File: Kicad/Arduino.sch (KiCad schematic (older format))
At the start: 5 parts

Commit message: Ready for Rev3 First layout review
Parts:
- removed D4: RGB_LED, ~, symbol RGB_LED
- added D4: LB_RGBLED, ~, symbol LB_RGBLED
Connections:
- wire segments 21 -> 26
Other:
- note added: "Changed model (3 units, pins = datasheet)"
- note added: "Connected 2nd Ard GND."
- moved on the sheet: R13, R14
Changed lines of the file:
@@
 Sheet 3 7
 Title ""
-Date "11 oct 2014"
+Date "18 oct 2014"
 Rev ""
 Comp ""
@@
 Text HLabel 2500 3550 0    60   Output ~ 0
 PumpDown
-Text HLabel 6400 3800 2    60   Output ~ 0
+Text HLabel 6400 2800 2    60   Output ~ 0
 ~RESET
-Text HLabel 6450 4200 2    60   Input ~ 0
+Text HLabel 6450 3000 2    60   Input ~ 0
 ~DR
 Wire Wire Line
-	5750 4200 6450 4200
+	5750 3000 6450 3000
 Text HLabel 2500 2450 0    60   Output ~ 0
 V+_ARD
@@
 	2500 3750 3550 3750
 Wire Wire Line
-	5750 3800 6400 3800
-$Comp
-L RGB_LED D4
-U 1 1 540F4D9B
-P 1750 4250
-F 0 "D4" H 1850 4600 50  0000 L CNN
-F 1 "RGB_LED" H 1750 3650 50  0000 C CNN
-F 2 "~" H 1750 4250 60  0000 C CNN
-F 3 "~" H 1750 4250 60  0000 C CNN
-	1    1750 4250
-	1    0    0    1
-$EndComp
+	5750 2800 6400 2800
 $Comp
 L R R14
 U 1 1 540F4E5D
-P 2850 4150
-F 0 "R14" V 2930 4150 40  0000 C CNN
-F 1 "499" V 2857 4151 40  0000 C CNN
-F 2 "~" V 2780 4150 30  0000 C CNN
-F 3 "~" H 2850 4150 30  0000 C CNN
-	1    2850 4150
+P 2850 4350
+F 0 "R14" V 2930 4350 40  0000 C CNN
+F 1 "499" V 2857 4351 40  0000 C CNN
+F 2 "~" V 2780 4350 30  0000 C CNN
+F 3 "~" H 2850 4350 30  0000 C CNN
+	1    2850 4350
 	0    -1   -1   0
 $EndComp
@@
 L R R13
 U 1 1 540F4E9E
-P 2850 4350
-F 0 "R13" V 2930 4350 40  0000 C CNN
-F 1 "499" V 2857 4351 40  0000 C CNN
-F 2 "~" V 2780 4350 30  0000 C CNN
-F 3 "~" H 2850 4350 30  0000 C CNN
-	1    2850 4350
+P 2850 4750
+F 0 "R13" V 2930 4750 40  0000 C CNN
+F 1 "499" V 2857 4751 40  0000 C CNN
+F 2 "~" V 2780 4750 30  0000 C CNN
+F 3 "~" H 2850 4750 30  0000 C CNN
+	1    2850 4750
 	0    -1   -1   0
 $EndComp
@@
 	3550 3950 3100 3950
 Wire Wire Line
-	2600 3950 2100 3950
+	1900 3950 2600 3950
 Wire Wire Line
-	2600 4150 2100 4150
+	1900 4350 2600 4350
 Wire Wire Line
-	2600 4350 2100 4350
+	1900 4750 2600 4750
+Text HLabel 950  4350 0    60   Output ~ 0
+V+_ARD
+$Comp
+L LB_RGBLED D4
+U 1 1 544128B0
+P 1700 3950
+F 0 "D4" H 1700 4050 50  0000 C CNN
+F 1 "LB_RGBLED" H 1700 3850 50  0000 C CNN
+F 2 "~" H 1700 3950 60  0000 C CNN
+F 3 "~" H 1700 3950 60  0000 C CNN
+	1    1700 3950
+	1    0    0    -1
+$EndComp
+$Comp
+L LB_RGBLED D4
+U 2 1 544128BD
+P 1700 4350
+F 0 "D4" H 1700 4450 50  0000 C CNN
+F 1 "LB_RGBLED" H 1700 4250 50  0000 C CNN
+F 2 "~" H 1700 4350 60  0000 C CNN
+F 3 "~" H 1700 4350 60  0000 C CNN
+	2    1700 4350
+	1    0    0    -1
+$EndComp
+$Comp
+L LB_RGBLED D4
+U 3 1 544128C3
+P 1700 4750
+F 0 "D4" H 1700 4850 50  0000 C CNN
+F 1 "LB_RGBLED" H 1700 4650 50  0000 C CNN
+F 2 "~" H 1700 4750 60  0000 C CNN
+F 3 "~" H 1700 4750 60  0000 C CNN
+	3    1700 4750
+	1    0    0    -1
+$EndComp
 Wire Wire Line
-	1350 4150 1200 4150
-Text HLabel 1200 4150 0    60   Output ~ 0
-V+_ARD
+	950  4350 1500 4350
 Wire Wire Line
-	3100 4150 3200 4150
+	1050 3950 1050 4750
 Wire Wire Line
-	3200 4150 3200 4350
+	1050 3950 1500 3950
+Connection ~ 1050 4350
 Wire Wire Line
-	3200 4350 3550 4350
+	1050 4750 1500 4750
+Text Notes 2700 5050 2    60   ~ 0
+Changed model (3 units, pins = datasheet)
 Wire Wire Line
-	3100 4350 3100 4250
+	3550 2850 3300 2850
 Wire Wire Line
-	3100 4250 3550 4250
+	3300 2850 3300 2650
+Connection ~ 3300 2650
+Text Notes 3450 3000 2    60   ~ 0
+Connected 2nd Ard GND.
 Wire Wire Line
-	3550 4250 3550 4150
+	3400 4750 3100 4750
+Wire Wire Line
+	3100 4350 3150 4350
+Wire Wire Line
+	3150 4350 3150 4150
+Wire Wire Line
+	3150 4150 3550 4150
+Wire Wire Line
+	3400 4750 3400 4350
+Wire Wire Line
+	3400 4350 3550 4350
 $EndSCHEMATC

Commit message: updated based on feedback. Ready for second review
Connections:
- net ~DR: now also ARD1.20 (PWM0); no longer ARD1.19 (Digital8)
- net ~RESET: now also ARD1.19 (Digital8); no longer ARD1.20 (PWM0)
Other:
- note removed: "Changed model (3 units, pins = datasheet)"
- note removed: "Connected 2nd Ard GND."
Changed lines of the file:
@@
 $Descr A4 11693 8268
 encoding utf-8
-Sheet 3 7
+Sheet 7 7
 Title ""
-Date "18 oct 2014"
+Date "21 oct 2014"
 Rev ""
 Comp ""
@@
 Text HLabel 2500 3550 0    60   Output ~ 0
 PumpDown
-Text HLabel 6400 2800 2    60   Output ~ 0
+Text HLabel 6350 3000 2    60   Output ~ 0
 ~RESET
-Text HLabel 6450 3000 2    60   Input ~ 0
-~DR
-Wire Wire Line
-	5750 3000 6450 3000
 Text HLabel 2500 2450 0    60   Output ~ 0
 V+_ARD
@@
 Wire Wire Line
 	2500 3750 3550 3750
-Wire Wire Line
-	5750 2800 6400 2800
 $Comp
 L R R14
@@
 Wire Wire Line
 	1050 4750 1500 4750
-Text Notes 2700 5050 2    60   ~ 0
-Changed model (3 units, pins = datasheet)
 Wire Wire Line
 	3550 2850 3300 2850
@@
 	3300 2850 3300 2650
 Connection ~ 3300 2650
-Text Notes 3450 3000 2    60   ~ 0
-Connected 2nd Ard GND.
 Wire Wire Line
 	3400 4750 3100 4750
@@
 Wire Wire Line
 	3400 4350 3550 4350
+Wire Wire Line
+	5750 3000 6350 3000
+Text HLabel 6350 2800 2    60   Input ~ 0
+~DR
+Wire Wire Line
+	5750 2800 6350 2800
 $EndSCHEMATC

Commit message: before changing ADC
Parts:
- removed ARD1: ARDUINOPINS, ~, symbol ARDUINOPINS
- added ARD?: ARDUINOPINS, ~, symbol ARDUINOPINS
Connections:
- net GND_ARD: now also ARD?.2 (GND), ARD?.3 (GND)
- net MISO: now also ARD?.23 (MISO)
- net MOSI: now also ARD?.22 (MOSI)
- net PumpDown: now also ARD?.5 (AnalogIn0)
- net PumpUp: now also ARD?.6 (AnalogIn1)
- net SCLK: now also ARD?.24 (SCK)
- net V+_ARD: now also ARD?.1 (5V)
- net ~CS: now also ARD?.21 (CS_N)
- net ~DR: now also ARD?.20 (PWM0)
- net ~RESET: now also ARD?.19 (Digital8)
- net at R12.2: now also ARD?.7 (AnalogIn2)
- net at R14.2: now also ARD?.8 (AnalogIn3)
- net at R13.2: now also ARD?.9 (SDA)
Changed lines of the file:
@@
 Sheet 7 7
 Title ""
-Date "21 oct 2014"
+Date "10 nov 2014"
 Rev ""
 Comp ""
@@
 Wire Wire Line
 	3550 2450 2500 2450
-$Comp
-L ARDUINOPINS ARD1
-U 1 1 53E0F48C
-P 4650 3150
-F 0 "ARD1" H 4000 4750 60  0000 C CNN
-F 1 "ARDUINOPINS" H 4150 4950 60  0000 C CNN
-F 2 "~" H 5200 2200 60  0000 C CNN
-F 3 "~" H 5200 2200 60  0000 C CNN
-	1    4650 3150
-	1    0    0    -1
-$EndComp
 Text HLabel 2500 2650 0    60   Input ~ 0
 GND_ARD
@@
 Wire Wire Line
 	5750 2800 6350 2800
+$Comp
+L ARDUINOPINS ARD?
+U 1 1 545EEF21
+P 4650 3150
+F 0 "ARD?" H 4000 4750 60  0000 C CNN
+F 1 "ARDUINOPINS" H 4150 4950 60  0000 C CNN
+F 2 "~" H 5200 2200 60  0000 C CNN
+F 3 "~" H 5200 2200 60  0000 C CNN
+	1    4650 3150
+	1    0    0    -1
+$EndComp
 $EndSCHEMATC

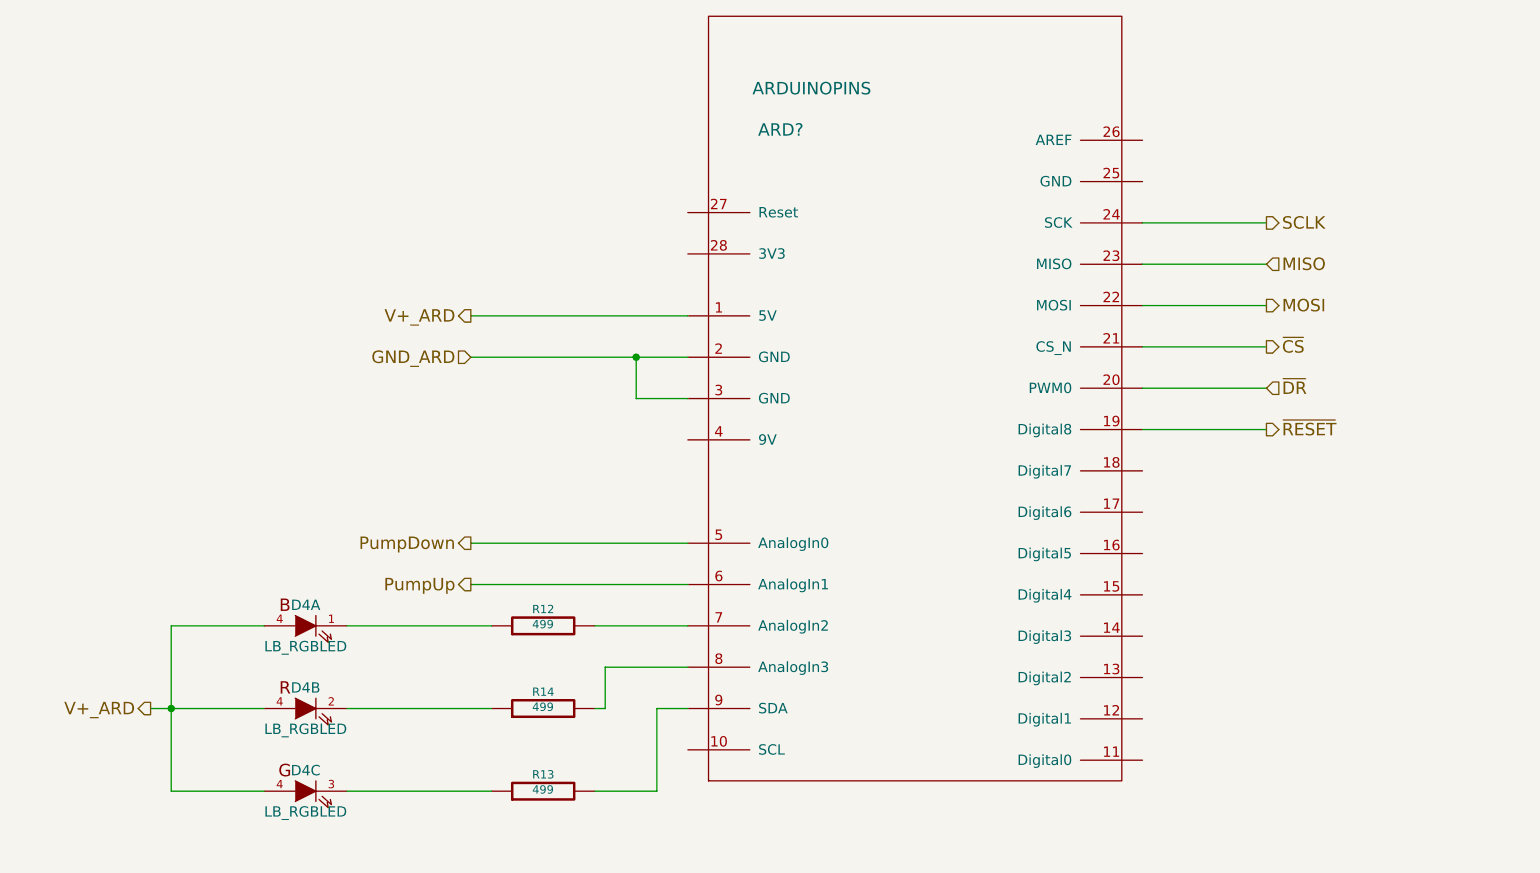
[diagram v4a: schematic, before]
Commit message: first pass changing ADC
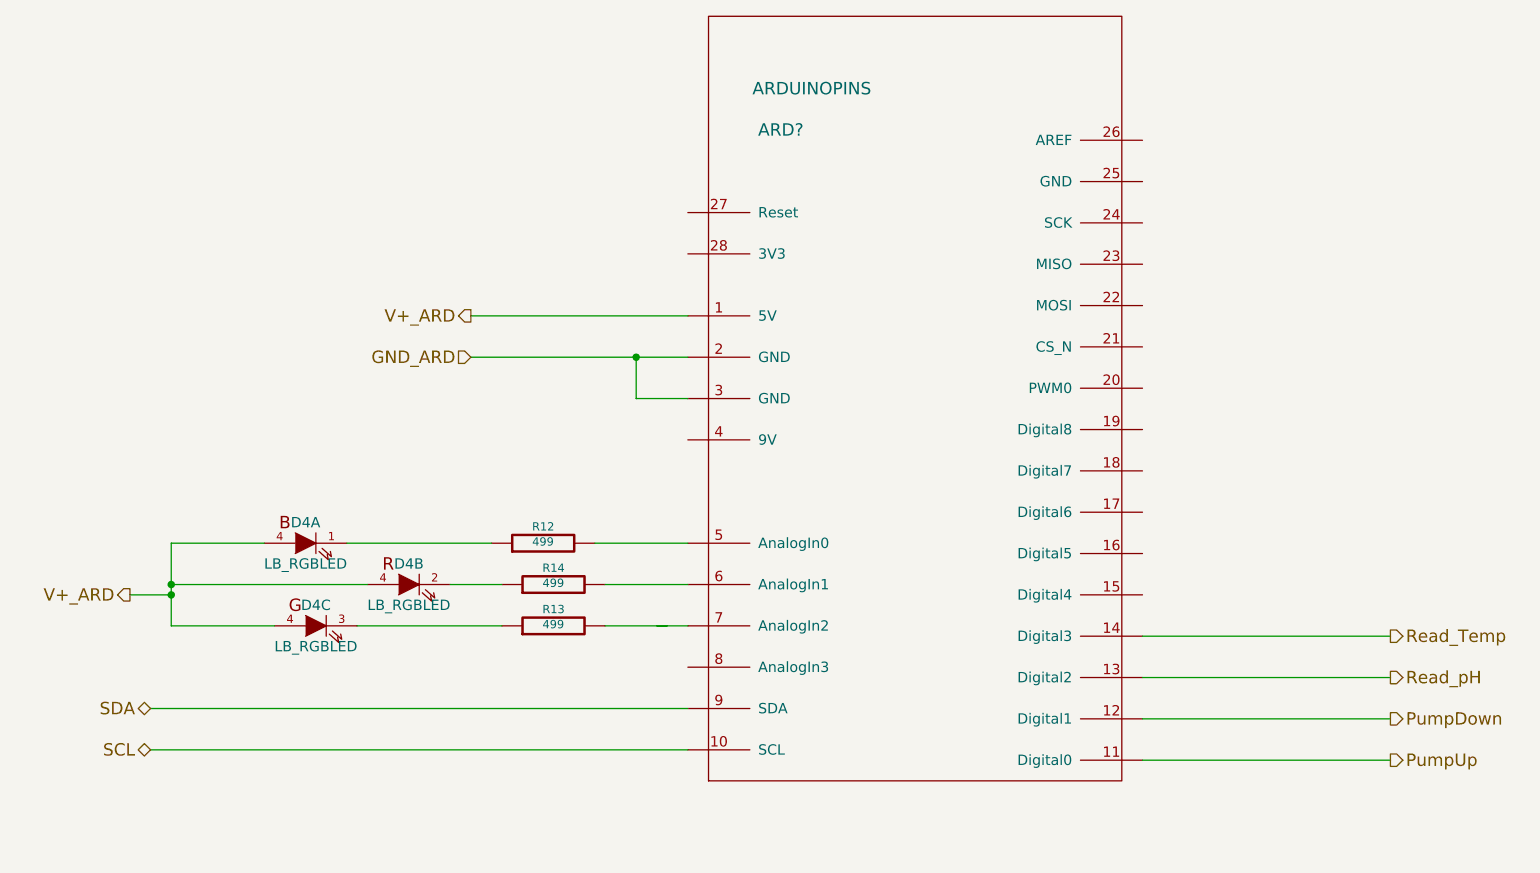
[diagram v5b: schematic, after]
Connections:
- net labels added: Read_Temp, Read_pH, SCL, SDA
- net labels removed: MISO, MOSI, SCLK, ~CS, ~DR, ~RESET
- wire segments 26 -> 22
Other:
- moved on the sheet: D4A, D4B, D4C, R12, R13, R14
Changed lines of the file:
@@
 $Descr A4 11693 8268
 encoding utf-8
-Sheet 7 7
+Sheet 6 7
 Title ""
-Date "10 nov 2014"
+Date "11 nov 2014"
 Rev ""
 Comp ""
@@
 Comment4 ""
 $EndDescr
-Text HLabel 6350 2000 2    60   Output ~ 0
-SCLK
-Wire Wire Line
-	6350 2000 5750 2000
-Text HLabel 6350 2200 2    60   Input ~ 0
-MISO
-Text HLabel 6350 2400 2    60   Output ~ 0
-MOSI
-Text HLabel 6350 2600 2    60   Output ~ 0
-~CS
-Wire Wire Line
-	5750 2200 6350 2200
-Wire Wire Line
-	5750 2400 6350 2400
-Text HLabel 2500 3550 0    60   Output ~ 0
-PumpDown
-Text HLabel 6350 3000 2    60   Output ~ 0
-~RESET
 Text HLabel 2500 2450 0    60   Output ~ 0
 V+_ARD
@@
 Wire Wire Line
 	2500 2650 3550 2650
-Wire Wire Line
-	3550 3550 2500 3550
-Text HLabel 2500 3750 0    60   Output ~ 0
+Text HLabel 6950 4600 2    60   Output ~ 0
 PumpUp
-Wire Wire Line
-	2500 3750 3550 3750
 $Comp
 L R R14
 U 1 1 540F4E5D
-P 2850 4350
-F 0 "R14" V 2930 4350 40  0000 C CNN
-F 1 "499" V 2857 4351 40  0000 C CNN
-F 2 "~" V 2780 4350 30  0000 C CNN
-F 3 "~" H 2850 4350 30  0000 C CNN
-	1    2850 4350
+P 2900 3750
+F 0 "R14" V 2980 3750 40  0000 C CNN
+F 1 "499" V 2907 3751 40  0000 C CNN
+F 2 "~" V 2830 3750 30  0000 C CNN
+F 3 "~" H 2900 3750 30  0000 C CNN
+	1    2900 3750
 	0    -1   -1   0
 $EndComp
@@
 L R R13
 U 1 1 540F4E9E
-P 2850 4750
-F 0 "R13" V 2930 4750 40  0000 C CNN
-F 1 "499" V 2857 4751 40  0000 C CNN
-F 2 "~" V 2780 4750 30  0000 C CNN
-F 3 "~" H 2850 4750 30  0000 C CNN
-	1    2850 4750
+P 2900 3950
+F 0 "R13" V 2980 3950 40  0000 C CNN
+F 1 "499" V 2907 3951 40  0000 C CNN
+F 2 "~" V 2830 3950 30  0000 C CNN
+F 3 "~" H 2900 3950 30  0000 C CNN
+	1    2900 3950
 	0    -1   -1   0
 $EndComp
@@
 L R R12
 U 1 1 540F4F03
-P 2850 3950
-F 0 "R12" V 2930 3950 40  0000 C CNN
-F 1 "499" V 2857 3951 40  0000 C CNN
-F 2 "~" V 2780 3950 30  0000 C CNN
-F 3 "~" H 2850 3950 30  0000 C CNN
-	1    2850 3950
+P 2850 3550
+F 0 "R12" V 2930 3550 40  0000 C CNN
+F 1 "499" V 2857 3551 40  0000 C CNN
+F 2 "~" V 2780 3550 30  0000 C CNN
+F 3 "~" H 2850 3550 30  0000 C CNN
+	1    2850 3550
 	0    -1   -1   0
 $EndComp
 Wire Wire Line
-	5750 2600 6350 2600
+	3550 3550 3100 3550
 Wire Wire Line
-	3550 3950 3100 3950
+	1900 3550 2600 3550
 Wire Wire Line
-	1900 3950 2600 3950
-Wire Wire Line
-	1900 4350 2600 4350
-Wire Wire Line
-	1900 4750 2600 4750
-Text HLabel 950  4350 0    60   Output ~ 0
+	1950 3950 2650 3950
+Text HLabel 850  3800 0    60   Output ~ 0
 V+_ARD
 $Comp
 L LB_RGBLED D4
 U 1 1 544128B0
-P 1700 3950
-F 0 "D4" H 1700 4050 50  0000 C CNN
-F 1 "LB_RGBLED" H 1700 3850 50  0000 C CNN
-F 2 "~" H 1700 3950 60  0000 C CNN
-F 3 "~" H 1700 3950 60  0000 C CNN
-	1    1700 3950
+P 1700 3550
+F 0 "D4" H 1700 3650 50  0000 C CNN
+F 1 "LB_RGBLED" H 1700 3450 50  0000 C CNN
+F 2 "~" H 1700 3550 60  0000 C CNN
+F 3 "~" H 1700 3550 60  0000 C CNN
+	1    1700 3550
 	1    0    0    -1
 $EndComp
@@
 L LB_RGBLED D4
 U 2 1 544128BD
-P 1700 4350
-F 0 "D4" H 1700 4450 50  0000 C CNN
-F 1 "LB_RGBLED" H 1700 4250 50  0000 C CNN
-F 2 "~" H 1700 4350 60  0000 C CNN
-F 3 "~" H 1700 4350 60  0000 C CNN
-	2    1700 4350
+P 2200 3750
+F 0 "D4" H 2200 3850 50  0000 C CNN
+F 1 "LB_RGBLED" H 2200 3650 50  0000 C CNN
+F 2 "~" H 2200 3750 60  0000 C CNN
+F 3 "~" H 2200 3750 60  0000 C CNN
+	2    2200 3750
 	1    0    0    -1
 $EndComp
@@
 L LB_RGBLED D4
 U 3 1 544128C3
-P 1700 4750
-F 0 "D4" H 1700 4850 50  0000 C CNN
-F 1 "LB_RGBLED" H 1700 4650 50  0000 C CNN
-F 2 "~" H 1700 4750 60  0000 C CNN
-F 3 "~" H 1700 4750 60  0000 C CNN
-	3    1700 4750
+P 1750 3950
+F 0 "D4" H 1750 4050 50  0000 C CNN
+F 1 "LB_RGBLED" H 1750 3850 50  0000 C CNN
+F 2 "~" H 1750 3950 60  0000 C CNN
+F 3 "~" H 1750 3950 60  0000 C CNN
+	3    1750 3950
 	1    0    0    -1
 $EndComp
 Wire Wire Line
-	950  4350 1500 4350
+	1050 3550 1500 3550
 Wire Wire Line
-	1050 3950 1050 4750
-Wire Wire Line
-	1050 3950 1500 3950
-Connection ~ 1050 4350
-Wire Wire Line
-	1050 4750 1500 4750
+	1050 3950 1550 3950
 Wire Wire Line
 	3550 2850 3300 2850
@@
 Connection ~ 3300 2650
 Wire Wire Line
-	3400 4750 3100 4750
+	3450 3950 3150 3950
 Wire Wire Line
-	3100 4350 3150 4350
+	3150 3750 3550 3750
 Wire Wire Line
-	3150 4350 3150 4150
-Wire Wire Line
-	3150 4150 3550 4150
-Wire Wire Line
-	3400 4750 3400 4350
-Wire Wire Line
-	3400 4350 3550 4350
-Wire Wire Line
-	5750 3000 6350 3000
-Text HLabel 6350 2800 2    60   Input ~ 0
-~DR
-Wire Wire Line
-	5750 2800 6350 2800
+	3400 3950 3550 3950
 $Comp
 L ARDUINOPINS ARD?
@@
 	1    0    0    -1
 $EndComp
+Wire Wire Line
+	5750 4600 6950 4600
+Text HLabel 6950 4400 2    60   Output ~ 0
+PumpDown
+Wire Wire Line
+	6950 4400 5750 4400
+Wire Wire Line
+	2650 3750 2400 3750
+Wire Wire Line
+	2000 3750 1050 3750
+Wire Wire Line
+	1050 3550 1050 3950
+Connection ~ 1050 3750
+Text HLabel 950  4350 0    60   BiDi ~ 0
+SDA
+Wire Wire Line
+	3550 4350 950  4350
+Wire Wire Line
+	3550 4550 950  4550
+Text HLabel 950  4550 0    60   BiDi ~ 0
+SCL
+Text HLabel 6950 4200 2    60   Output ~ 0
+Read_pH
+Wire Wire Line
+	5750 4200 6950 4200
+Text HLabel 6950 4000 2    60   Output ~ 0
+Read_Temp
+Wire Wire Line
+	5750 4000 6950 4000
+Wire Wire Line
+	850  3800 1050 3800
+Connection ~ 1050 3800
 $EndSCHEMATC
